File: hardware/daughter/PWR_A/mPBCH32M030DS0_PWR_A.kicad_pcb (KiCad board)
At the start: 2 copper layers, 60 x 42 mm, 76 parts, among them J1 B2B_PWR, J2 OUT0, J3 B2B_SIG, J4 OUT1, J5 OUT2, J6 OUT3, Q1 TPN1R603PL, Q2 TPN1R603PL, Q3 TPN1R603PL, Q4 TPN1R603PL, Q5 TPN1R603PL, Q6 TPN1R603PL, Q7 TPN1R603PL, Q8 TPN1R603PL

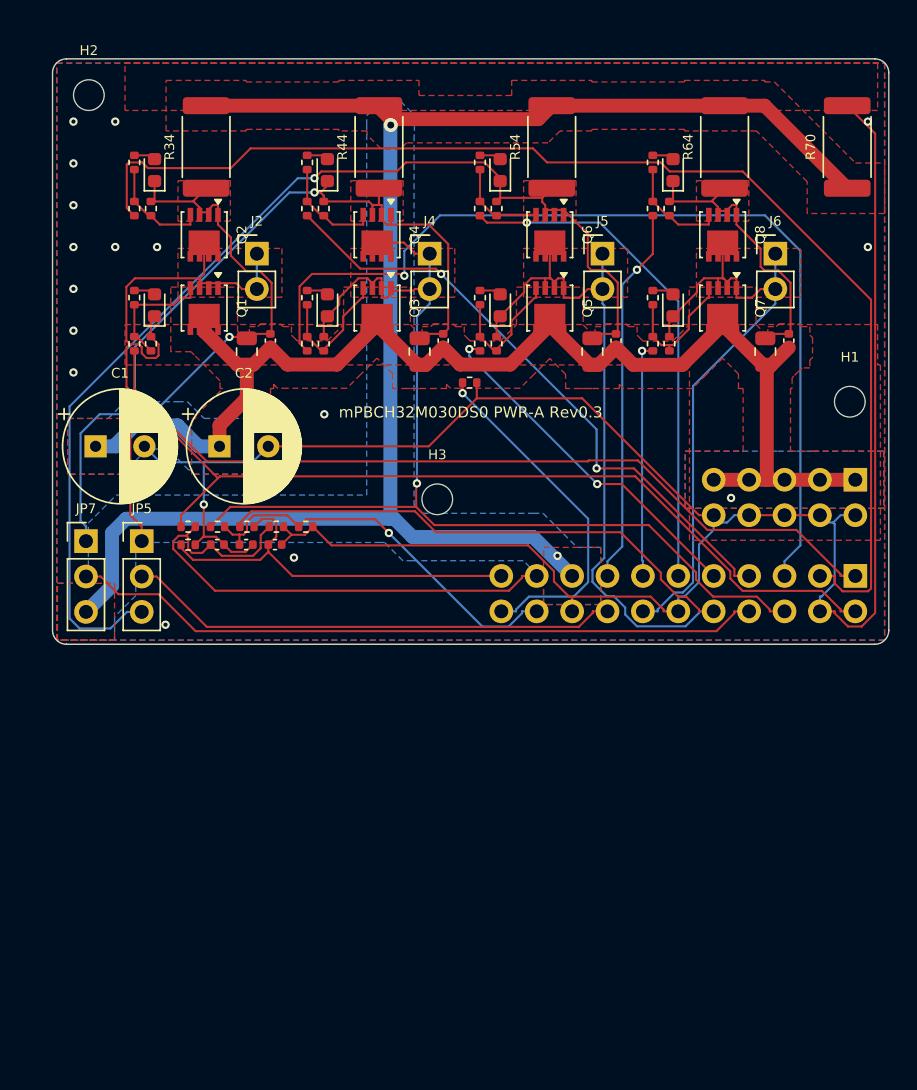
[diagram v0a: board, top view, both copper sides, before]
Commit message: Rev 0.4: DIP-42 MCU module + power boards A/B/C (KiCad 8)
- MCU module: 20.32 x 53.34mm (8 x 21 grid), DIP-42 (0.6in rows), fits
  an 82 x 52mm breadboard. Headers can be fitted from either side;
  signal names on bottom silk. All LEDs (power, status, 8 gate LEDs) on
  the module top.
- Power boards take the module in two 1x21 sockets (left/right
  symmetric mating). FETs/shunts on the heatsink side, no LEDs.
  Voltage-dependent parts (TVS, OVP divider, bulk caps, BEMF divider)
  moved to the power boards. Breakout board D removed.
  A/C: 20.32 x 71.94mm, B (TO-263 x8): 40.64 x 66.94mm.
- Capacitors re-selected for realistic size vs voltage/capacitance
  (4.7uF 1608, 10uF/25V 2012, 10uF/50V 1206, 4.7nF/100V 1608, low
  profile electrolytics).
- Schematics and boards generated in KiCad 8 format; netlists verified
  with KiCad 8.0.9.
- Layout pipeline: Freerouting bridge (parallel), second pass, early
  repair before pours, island-aware maze repair, DRC via kicad-cli.
- DRC: power boards A/B/C have 0 unconnected / 0 electrical errors.
  The MCU module still has unrouted connections (work in progress).

Co-Authored-By: Claude Opus 5.5 <noreply@anthropic.com>
Claude-Session: https://claude.ai/code/session_01LENFjjhDfYjJZV1NWhB9uV
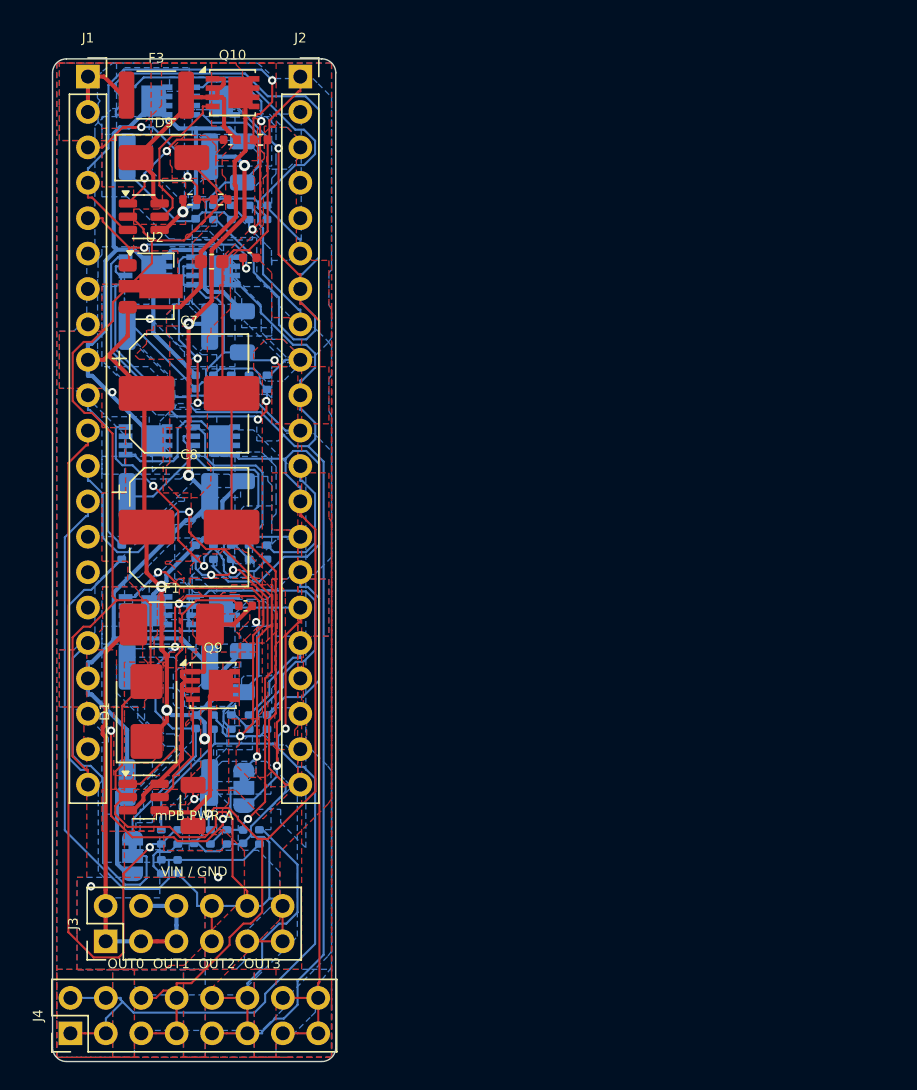
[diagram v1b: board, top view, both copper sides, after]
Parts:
- removed C2: 470uF/25V, CP_Radial_D8.0mm_P3.50mm
- removed D10: RED GH0, LED_0603_1608Metric
- removed D11: GREEN GL0, LED_0603_1608Metric
- removed D12: RED GH1, LED_0603_1608Metric
- removed D13: GREEN GL1, LED_0603_1608Metric
- removed D14: RED GH2, LED_0603_1608Metric
- removed D15: GREEN GL2, LED_0603_1608Metric
- removed D16: RED GH3, LED_0603_1608Metric
- removed D17: GREEN GL3, LED_0603_1608Metric
- removed H1, H2, H3: M2, MountingHole_2.2mm_M2
- removed J5: OUT2, PinHeader_1x02_P2.54mm_Vertical
- removed J6: OUT3, PinHeader_1x02_P2.54mm_Vertical
- removed R35, R36, R45, R46, R55, R56, R65, R66: 22k, R_0402_1005Metric
- added C3: 1uF/50V, C_0603_1608Metric, F.Cu at (11.4, 14.5)
- added C4: 1uF/25V, C_0402_1005Metric, F.Cu at (14.1, 14.3)
- added C5: 0.1uF/50V, C_0402_1005Metric, F.Cu at (13.8, 39.2)
- added C6: 0.1uF/50V, C_0402_1005Metric, F.Cu at (12.7, 5.79)
- added C7: 100uF/25V, CP_Elec_8x6.2, F.Cu at (9.79, 24.0)
- added C8: 100uF/25V, CP_Elec_8x6.2, F.Cu at (9.79, 33.6)
- added D1: SMBJ16A, D_SMB, F.Cu at (6.75, 46.8)
- added D9: SMAJ20A, D_SMA, F.Cu at (8.00, 7.08)
- added F1: 10A, Fuse_Littelfuse_NANO2_2410, F.Cu at (8.54, 40.6)
- added F3: 5A, Fuse_1812_4532Metric, F.Cu at (7.45, 2.60)
- added Q10: TPN1R603PL, Vishay_PowerPAK_1212-8_Single, F.Cu at (12.9, 2.42)
- added Q9: TPN2R304PL, Vishay_PowerPAK_1212-8_Single, F.Cu at (11.5, 45.0)
- added R11: 110k 1%, R_0402_1005Metric, F.Cu at (9.87, 10.1)
- added R12: 10k 1%, R_0402_1005Metric, F.Cu at (12.1, 10.1)
- added R6: 100k, R_0402_1005Metric, F.Cu at (14.9, 5.80)
- added U2: 78L05, SOT-89-3, F.Cu at (7.34, 16.3)
- added U4: LM74700-Q1, SOT-23-6, F.Cu at (6.54, 53.0)
- added U5: LM74700-Q1, SOT-23-6, F.Cu at (6.54, 11.3)
- C1: value 470uF/25V -> 10uF/50V; footprint CP_Radial_D8.0mm_P3.50mm -> C_1206_3216Metric
- C30, C40, C50, C60, C71, C72, C73, Q1, Q2, Q3, Q4, Q5, Q6, Q7, Q8, R30, R31, R32, R33, R34, R40, R41, R42, R43, R44, R50, R51, R52, R53, R54, R60, R61, R62, R63, R64, R70, R71, R72, R74, R75, R77, R78, TH1: moved to B.Cu
- C31, C41, C51, C61: footprint C_0805_2012Metric -> C_1206_3216Metric; moved to B.Cu
- J1: value B2B_PWR -> SOCK_L; footprint PinSocket_2x05_P2.54mm_Vertical -> PinSocket_1x21_P2.54mm_Vertical; moved to F.Cu
- J2: value OUT0 -> SOCK_R; footprint PinHeader_1x02_P2.54mm_Vertical -> PinSocket_1x21_P2.54mm_Vertical
- J3: value B2B_SIG -> PWR_IN; footprint PinSocket_2x11_P2.54mm_Vertical -> PinHeader_2x06_P2.54mm_Vertical; moved to F.Cu
- J4: value OUT1 -> MOTOR; footprint PinHeader_1x02_P2.54mm_Vertical -> PinHeader_2x08_P2.54mm_Vertical
- JP5, JP7: footprint PinHeader_1x03_P2.54mm_Vertical -> SolderJumper-3_P1.3mm_Bridged12_RoundedPad1.0x1.5mm_NumberLabels; moved to B.Cu
- moved R70 66.7 mm to (8.31, 51.9), turned to 0 degrees
- moved J1 62.2 mm to (2.54, 1.27), turned to 0 degrees
- moved J4 61.6 mm to (1.28, 69.9), turned to 90 degrees
- moved J3 59.8 mm to (3.81, 63.3)
- moved Q7 44.0 mm to (6.67, 3.02), turned to 0 degrees
- moved C60 43.5 mm to (10.3, 11.0), turned to -90 degrees
- moved R64 39.9 mm to (8.31, 7.01), turned to 0 degrees
- moved C61 39.9 mm to (13.6, 7.39), turned to -90 degrees
- moved Q8 37.8 mm to (11.5, 3.02), turned to 0 degrees
- moved R32 37.8 mm to (14.1, 47.6), turned to -90 degrees
- moved R34 37.4 mm to (8.31, 43.6), turned to 0 degrees
- moved R33 37.3 mm to (12.8, 47.6), turned to -90 degrees
- moved R61 34.0 mm to (11.5, 11.0), turned to -90 degrees
- moved R63 31.4 mm to (12.8, 11.0), turned to -90 degrees
- moved R54 30.4 mm to (8.31, 19.2), turned to 0 degrees
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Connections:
- J1 pad 1: VBUS -> USB_VBUS
- J1 pad 10: GND -> NTC
- J1 pad 2: GND -> USB_VBUS
- J1 pad 3: VBUS -> VBUS_SNS
- J1 pad 4: GND -> PD_PWR_EN
- J1 pad 5: VBUS -> +5V
- J1 pad 6: GND -> +3V3
- J1 pad 7: VBUS -> SWDIO
- J1 pad 8: GND -> nRST
- J2 pad 1: SW0 -> GND
- J2 pad 2: SW0 -> UART_TX
- J3 pad 1: HO0 -> VIN
- J3 pad 10: SW2 -> GND
- J3 pad 11: LO2 -> GND
- J3 pad 2: SW0 -> VIN
- J3 pad 3: LO0 -> VIN
- J3 pad 4: GND -> VIN
- J3 pad 5: HO1 -> VIN
- J3 pad 6: SW1 -> VIN
- J3 pad 7: LO1 -> GND
- J3 pad 8: ISA_SEL -> GND
- J3 pad 9: HO2 -> GND
- J4 pad 1: SW1 -> SW0
- J4 pad 2: SW1 -> SW0
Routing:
- net LO0: track 87.8 -> 7.00 mm
- net SW3: track 46.5 -> 125.3 mm, vias 0 -> 1
- net VBUS: track 92.1 -> 161.9 mm, vias 1 -> 6
- net HO1: track 68.9 -> 9.98 mm, vias 1 -> 0
- net GND: track 160.5 -> 216.9 mm, vias 17 -> 2
- net ISH: track 119.6 -> 71.6 mm, vias 2 -> 3
- net HO0: track 60.2 -> 13.4 mm
- net LO1: track 44.4 -> 3.92 mm, vias 2 -> 0
- net VIN: track 0.00 -> 33.9 mm, vias 0 -> 1
- net LO2: track 36.5 -> 6.12 mm, vias 1 -> 0
- net PD_PWR_EN: track 0.00 -> 30.0 mm, vias 0 -> 1
- net ISA_SEL: track 49.9 -> 24.0 mm
- net SW2: track 88.7 -> 112.8 mm
- net SRC2: track 81.9 -> 59.3 mm, vias 1 -> 2
- net HO2: track 25.4 -> 2.85 mm, vias 2 -> 0
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- added copper zone on B.Cu, net SRC0
- added copper zone on B.Cu, net SRC1
- added copper zone on B.Cu, net SRC2
- added copper zone on B.Cu, net SRC3
- added copper zone on B.Cu, net SW0
- added copper zone on B.Cu, net SW1
- added copper zone on B.Cu, net SW2
- added copper zone on B.Cu, net SW3
- added copper zone on B.Cu, net USB_VBUS
- added copper zone on F.Cu, net USB_VBUS
- added copper zone on F.Cu, net USB_VBUS_P
- added copper zone on B.Cu, net VIN
- added copper zone on F.Cu, net VIN
- added copper zone on F.Cu, net VIN_F
- removed copper zone on F.Cu, net SRC3
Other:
- board size 60 x 42 mm -> 20.3 x 71.9 mm
- board text added: "OUT0 OUT1 OUT2 OUT3"
- board text added: "VIN / GND"
- board text added: "mPB PWR-A"
- board text removed: "mPBCH32M030DS0 PWR-A Rev0.3"

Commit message: Rev 0.4: rework module pinout for routability, power boards regenerated
- Module edge pin order follows the CH32M030 QFN48 pin sides so the
  breakout traces nest instead of crossing (J1: USB_VBUS, PD_PWR_EN,
  PC4/PC5, +3V3, +5V, SWDIO, VBUS, NTC, BEMF, HALL, ISx, TACH;
  J2: RX/TX, nRST, gate drive HO3..LO0, VBUS_SNS, I2C, nFAULT).
- Module: area under the QFN kept for fan-out (filters and the VHV/USB
  diode block moved away, gate LEDs right-aligned to J2).
- Power boards A/B/C re-placed for the new pinout (VBUS divider next to
  J2 VBUS_SNS, LM74700 next to its FET) and re-routed: all three at
  0 unconnected / 0 electrical DRC errors.
- Layout tooling: DRC via kicad-cli in a separate process, reload after
  SES import, selectable Freerouting jar, optional rip-up repair,
  configurable Freerouting timeout.
- MCU module still has unrouted connections (work in progress).

Co-Authored-By: Claude Opus 5.5 <noreply@anthropic.com>
Claude-Session: https://claude.ai/code/session_01LENFjjhDfYjJZV1NWhB9uV
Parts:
- moved R11 29.5 mm to (5.42, 39.3)
- moved R12 29.5 mm to (7.62, 39.3)
- moved C3 4.31 mm to (10.4, 10.4)
- moved C4 4.31 mm to (13.1, 10.1)
- moved F1 1.73 mm to (8.54, 42.3)
- moved C1 1.73 mm to (10.1, 55.3)
- moved C5 1.73 mm to (13.8, 41.0)
- moved D1 1.73 mm to (6.75, 48.6)
- moved Q9 1.73 mm to (11.5, 46.7)
- moved U4 1.73 mm to (6.54, 54.7)
- moved C73 0.40 mm to (8.97, 57.6)
- moved R70 0.40 mm to (8.31, 51.5)
- moved C71 0.40 mm to (10.2, 55.4)
- moved C72 0.40 mm to (13.7, 55.4)
- moved JP5 0.40 mm to (13.7, 51.9)
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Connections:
- J1 pad 3: VBUS_SNS -> PD_PWR_EN
- J1 pad 4: PD_PWR_EN -> GPIO_PC4
- J1 pad 5: +5V -> GPIO_PC5
- J1 pad 7: SWDIO -> +5V
- J1 pad 8: nRST -> SWDIO
- J2 pad 10: SW2 -> LO2
- J2 pad 11: LO2 -> HO1
- J2 pad 12: HO1 -> SW1
- J2 pad 13: SW1 -> LO1
- J2 pad 14: LO1 -> HO0
- J2 pad 15: HO0 -> SW0
- J2 pad 16: SW0 -> LO0
- J2 pad 17: LO0 -> VBUS_SNS
- J2 pad 18: I2C_SDA -> I2C_SCL
- J2 pad 19: I2C_SCL -> I2C_SDA
- J2 pad 2: UART_TX -> UART_RX
- J2 pad 3: UART_RX -> UART_TX
- J2 pad 4: GPIO_PC4 -> nRST
- J2 pad 5: GPIO_PC5 -> HO3
- J2 pad 6: HO3 -> SW3
- J2 pad 7: SW3 -> LO3
- J2 pad 8: LO3 -> HO2
- J2 pad 9: HO2 -> SW2
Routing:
- net GND: track 216.9 -> 184.4 mm, vias 2 -> 5
- net BEMF_V: track 43.2 -> 71.6 mm, vias 2 -> 1
- net SW2: track 112.8 -> 87.0 mm, vias 0 -> 2
- net SW3: track 125.3 -> 105.0 mm, vias 1 -> 2
- net +5V: track 15.9 -> 33.0 mm, vias 2 -> 1
- net BEMF_U: track 53.5 -> 36.6 mm
- net SW1: track 94.1 -> 77.2 mm, vias 1 -> 2
- net SW0: track 80.2 -> 70.6 mm, vias 1 -> 3
- net ISB_SEL: track 21.7 -> 30.8 mm, vias 2 -> 3
- net ISH: track 71.6 -> 78.5 mm
- net VBUS: track 161.9 -> 155.4 mm
- net GL0: track 22.4 -> 16.0 mm
- net PD_PWR_EN: track 30.0 -> 23.7 mm, vias 1 -> 0
- net GH0: track 27.0 -> 33.1 mm, vias 2 -> 0
- net GL1: track 15.3 -> 21.0 mm
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- removed copper zone on F.Cu, net SRC2

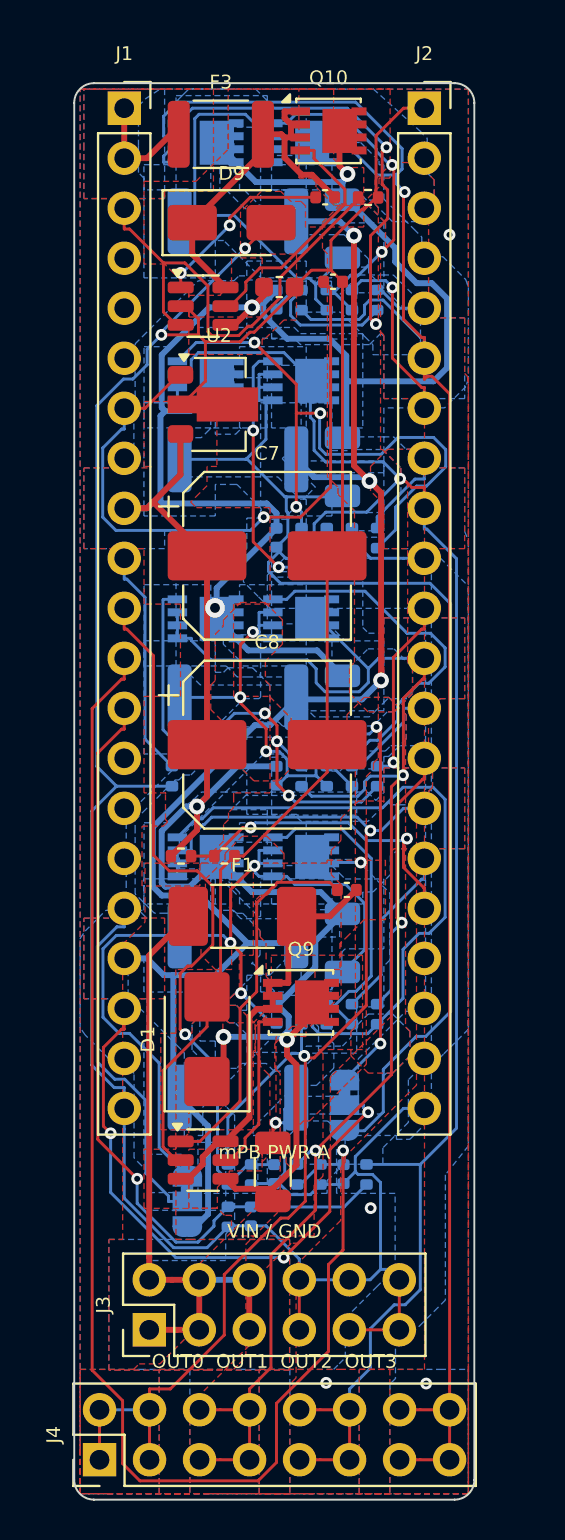
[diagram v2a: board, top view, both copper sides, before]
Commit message: 9マス版に一本化 (8マス版を削除)
- 8 マス版 (20.32mm) は JLCPCB の 2 層標準 0.127mm で配線しきれないため削除
- 9 マス版 (22.86mm, 端子列 0.7in) を hardware/ 直下・hardware/daughter/・hardware/fab/・docs/pcb/ へ移動
- ベタなし版は hardware/nopour/ (図は docs/pcb/nopour/)
- gen_pcb.py から MPB_W9 の切り替えを外し 9 マス固定に。既定ルールは 0.127mm / ビア 0.6/0.3
  (再生成した配置が確定済みの 4 基板と一致することを確認)
- 回路図の注記 (外形・列間) を 22.86mm / 17.78mm に更新し PDF を再出力
- README / stacking.md / design.md を 9 マス版のみの記述に更新

Co-Authored-By: Claude Opus 5.5 <noreply@anthropic.com>
Claude-Session: https://claude.ai/code/session_01LENFjjhDfYjJZV1NWhB9uV
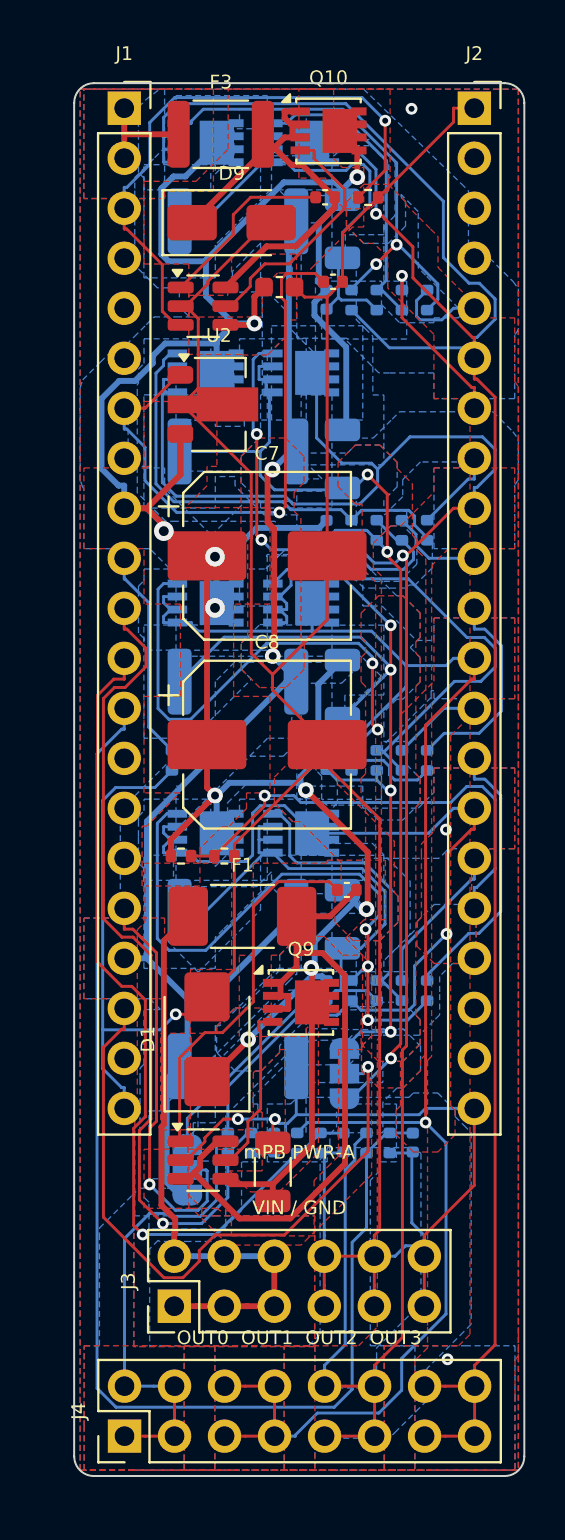
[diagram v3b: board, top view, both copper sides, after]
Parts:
- moved C73 9.03 mm to (17.2, 53.8)
- moved R78 9.03 mm to (16.0, 53.8)
- moved C30 2.81 mm to (12.8, 46.1)
- moved R30 2.81 mm to (17.9, 46.1)
- moved R31 2.81 mm to (14.1, 46.1)
- moved R33 2.81 mm to (15.4, 46.1)
- moved R32 2.81 mm to (16.6, 46.1)
- moved R40 2.66 mm to (17.9, 34.4)
- moved R41 2.66 mm to (14.1, 34.4)
- moved R43 2.66 mm to (15.4, 34.4)
- moved R42 2.66 mm to (16.6, 34.4)
- moved C40 2.66 mm to (12.8, 34.4)
- moved C50 2.57 mm to (12.8, 22.7)
- moved R50 2.57 mm to (17.9, 22.7)
- moved R51 2.57 mm to (14.1, 22.7)
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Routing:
- net BEMF_V: track 71.6 -> 44.2 mm
- net BEMF_W: track 40.5 -> 64.0 mm, vias 1 -> 0
- net SW2: track 87.0 -> 109.6 mm, vias 2 -> 1
- net VIN_F: track 21.0 -> 36.2 mm
- net ISH: track 78.5 -> 64.8 mm, vias 3 -> 2
- net SW1: track 77.2 -> 89.6 mm, vias 2 -> 1
- net SRC1: track 42.0 -> 54.1 mm, vias 5 -> 4
- net SRC0: track 46.4 -> 35.8 mm, vias 3 -> 0
- net SW3: track 105.0 -> 114.2 mm
- net GND: track 184.4 -> 193.5 mm, vias 5 -> 4
- net GH2: track 31.6 -> 23.0 mm, vias 3 -> 0
- net VBUS_SNS: track 16.2 -> 23.8 mm, vias 2 -> 1
- net SRC2: track 62.8 -> 55.2 mm, vias 0 -> 3
- net BEMF_U: track 36.6 -> 43.9 mm
- net GH1: track 24.5 -> 30.6 mm, vias 3 -> 2
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- added copper zone on F.Cu, net SRC2
- removed copper zone on F.Cu, net SRC0
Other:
- board size 20.3 x 71.9 mm -> 22.9 x 70.7 mm
